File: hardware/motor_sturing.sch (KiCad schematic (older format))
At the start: 6 parts, among them U1 LTC2351-14, U22 LTC2351-14, U5 MAX6101

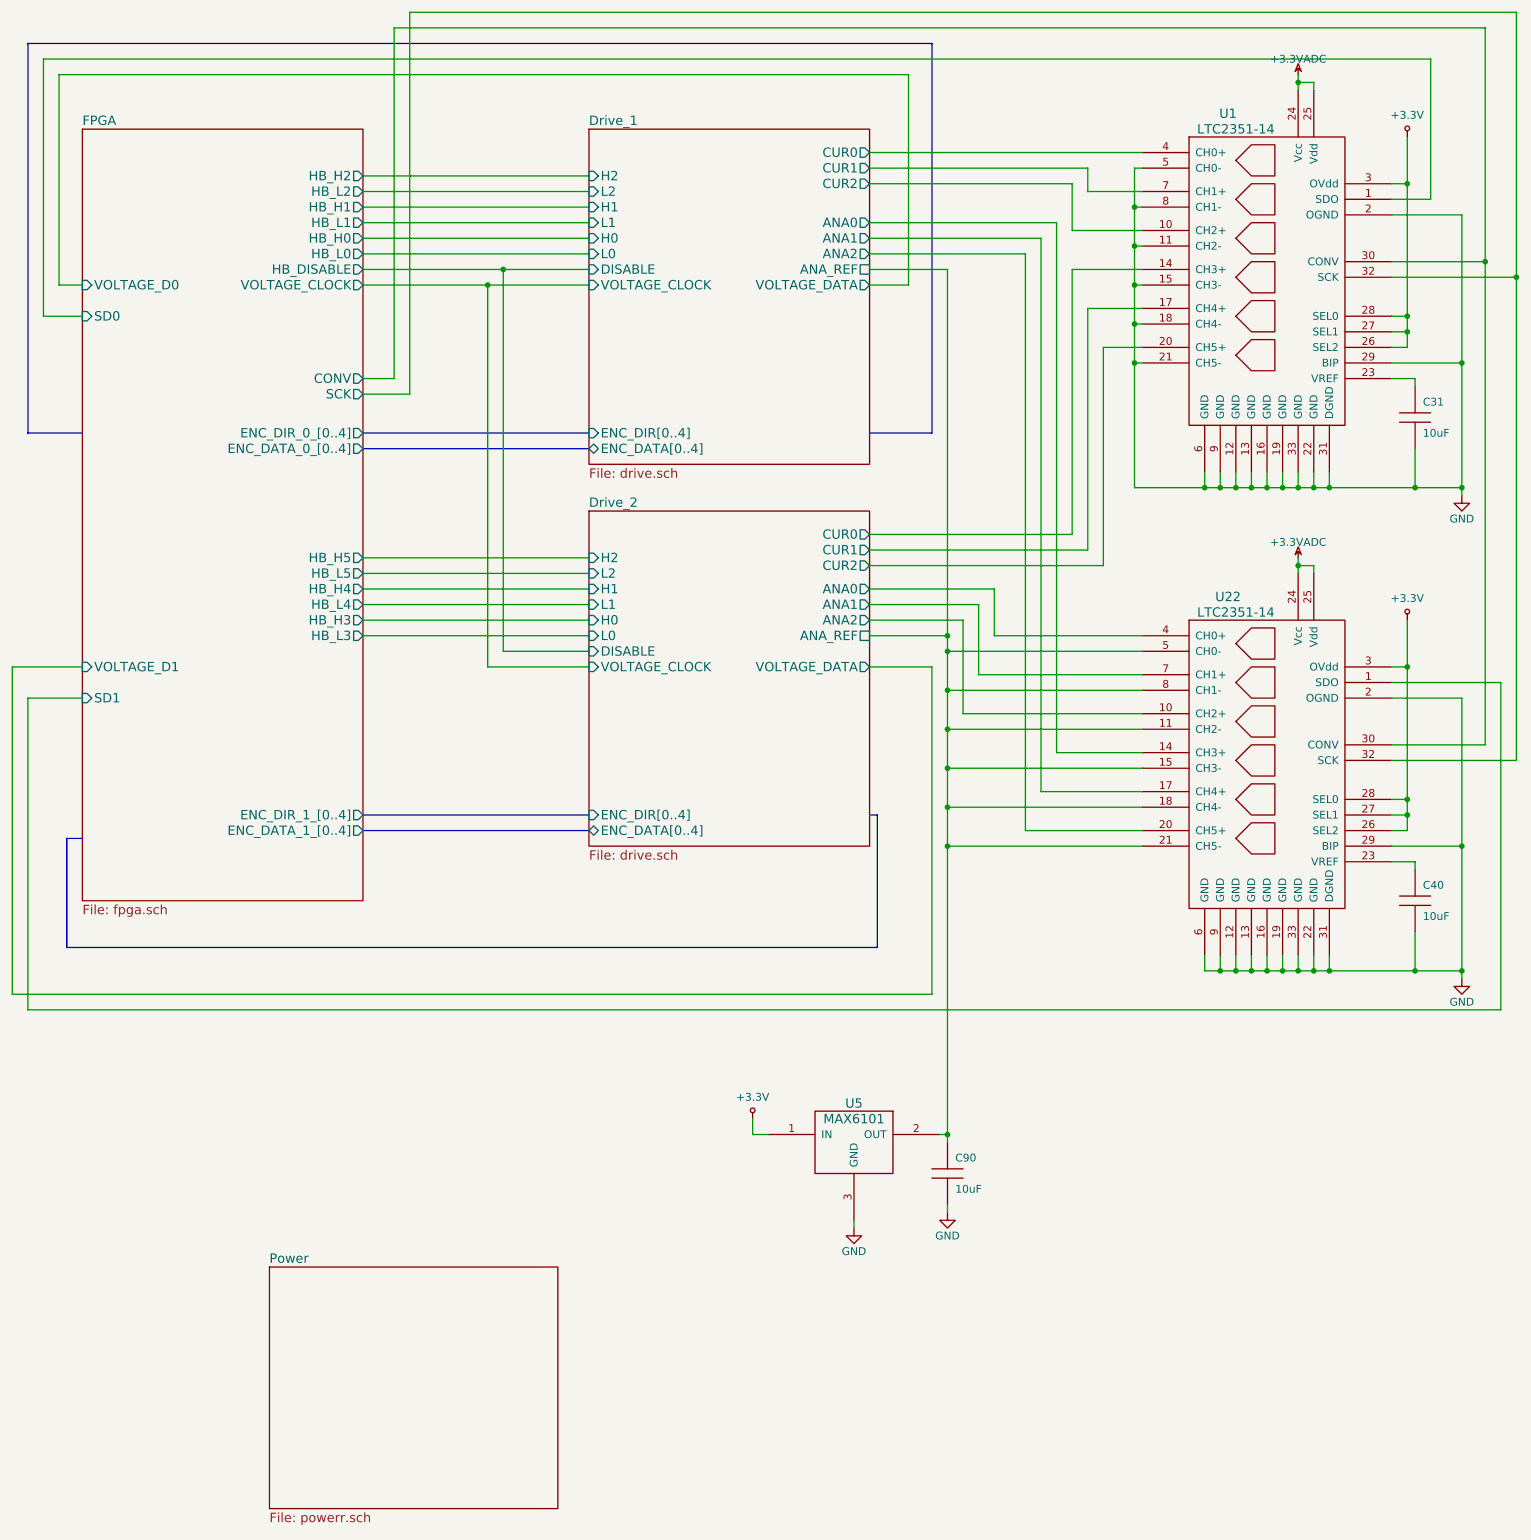
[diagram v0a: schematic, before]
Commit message: Backup, clearing bottom of power section.
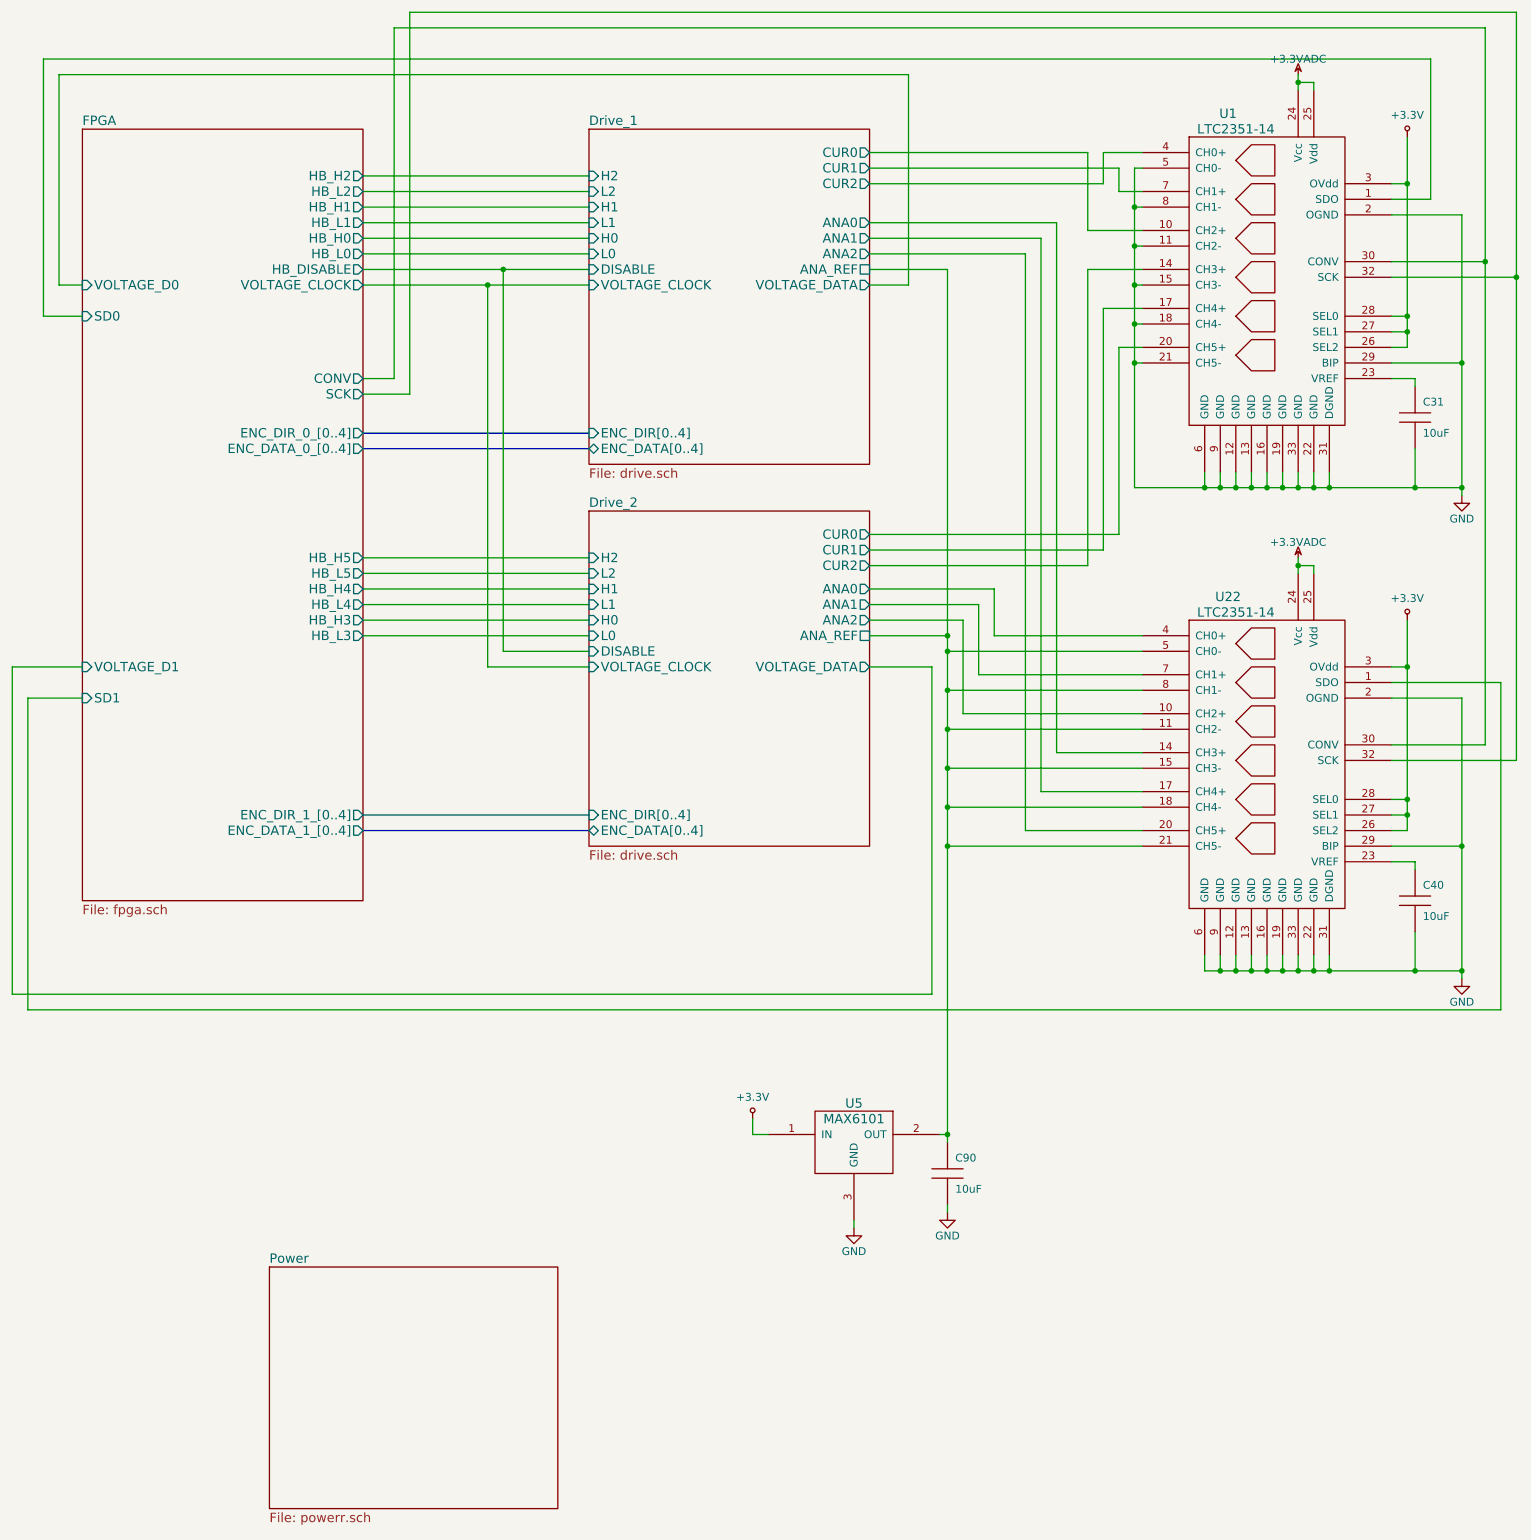
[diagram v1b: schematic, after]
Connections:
- net Drive_1/CUR0: now also U1.10 (CH2+); no longer U1.4 (CH0+)
- net Drive_1/CUR2: now also U1.4 (CH0+); no longer U1.10 (CH2+)
- net Drive_2/CUR0: now also U1.20 (CH5+); no longer U1.14 (CH3+)
- net Drive_2/CUR2: now also U1.14 (CH3+); no longer U1.20 (CH5+)
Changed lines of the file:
@@
 Wire Wire Line
 	4450 4700 5000 4700
-Wire Bus Line
-	6800 5750 6850 5750
-Wire Bus Line
-	6850 5750 6850 6600
-Wire Bus Line
-	6850 6600 1650 6600
-Wire Bus Line
-	1650 6600 1650 5900
-Wire Bus Line
-	1650 5900 1750 5900
 Wire Wire Line
 	1600 1000 1600 2350
@@
 Wire Wire Line
 	1500 2550 1750 2550
-Wire Bus Line
-	6800 3300 7200 3300
-Wire Bus Line
-	7200 3300 7200 800
-Wire Bus Line
-	7200 800  1400 800
-Wire Bus Line
-	1400 800  1400 3300
-Wire Bus Line
-	1400 3300 1750 3300
-Wire Wire Line
-	6800 1600 8200 1600
-Wire Wire Line
-	8200 1600 8200 1750
-Wire Wire Line
-	8200 1750 8550 1750
-Wire Wire Line
-	6800 1700 8100 1700
-Wire Wire Line
-	6800 3950 8100 3950
-Wire Wire Line
-	8100 3950 8100 2250
-Wire Wire Line
-	8100 2250 8550 2250
-Wire Wire Line
-	8100 1700 8100 2000
-Wire Wire Line
-	8100 2000 8550 2000
-Wire Wire Line
-	8550 2500 8200 2500
-Wire Wire Line
-	8200 2500 8200 4050
-Wire Wire Line
-	8200 4050 6800 4050
-Wire Wire Line
-	6800 4150 8300 4150
-Wire Wire Line
-	8300 4150 8300 2750
-Wire Wire Line
-	8300 2750 8550 2750
 Wire Wire Line
 	8550 1600 8500 1600
@@
 	8550 1850 8500 1850
 Connection ~ 8500 1850
-Wire Wire Line
-	8550 1500 6800 1500
-$Comp
-L +3.3VADC #PWR5
+$Comp
+L +3.3VADC #PWR198
 U 1 1 56D0AB8B
 P 9550 4100
-F 0 "#PWR5" H 9700 4050 50  0001 C CNN
+F 0 "#PWR198" H 9700 4050 50  0001 C CNN
 F 1 "+3.3VADC" H 9550 4200 50  0000 C CNN
 F 2 "" H 9550 4100 50  0000 C CNN
@@
 Connection ~ 9550 4150
 $Comp
-L +3.3V #PWR6
+L +3.3V #PWR199
 U 1 1 56D0BAED
 P 10250 1400
-F 0 "#PWR6" H 10250 1250 50  0001 C CNN
+F 0 "#PWR199" H 10250 1250 50  0001 C CNN
 F 1 "+3.3V" H 10250 1540 50  0000 C CNN
 F 2 "" H 10250 1400 50  0000 C CNN
@@
 	10250 1700 10150 1700
 $Comp
-L GND #PWR8
+L GND #PWR201
 U 1 1 56D0BF5F
 P 10600 3700
-F 0 "#PWR8" H 10600 3450 50  0001 C CNN
+F 0 "#PWR201" H 10600 3450 50  0001 C CNN
 F 1 "GND" H 10600 3550 50  0000 C CNN
 F 2 "" H 10600 3700 50  0000 C CNN
@@
 $EndComp
 $Comp
-L +3.3V #PWR7
+L +3.3V #PWR200
 U 1 1 56D10ACF
 P 10250 4500
-F 0 "#PWR7" H 10250 4350 50  0001 C CNN
+F 0 "#PWR200" H 10250 4350 50  0001 C CNN
 F 1 "+3.3V" H 10250 4640 50  0000 C CNN
 F 2 "" H 10250 4500 50  0000 C CNN
@@
 	10250 4800 10150 4800
 $Comp
-L GND #PWR9
+L GND #PWR202
 U 1 1 56D10AD7
 P 10600 6800
-F 0 "#PWR9" H 10600 6550 50  0001 C CNN
+F 0 "#PWR202" H 10600 6550 50  0001 C CNN
 F 1 "GND" H 10600 6650 50  0000 C CNN
 F 2 "" H 10600 6800 50  0000 C CNN
@@
 $EndComp
 $Comp
-L +3.3V #PWR1
+L +3.3V #PWR194
 U 1 1 56D1582B
 P 6050 7700
-F 0 "#PWR1" H 6050 7550 50  0001 C CNN
+F 0 "#PWR194" H 6050 7550 50  0001 C CNN
 F 1 "+3.3V" H 6050 7840 50  0000 C CNN
 F 2 "" H 6050 7700 50  0000 C CNN
@@
 	6050 7800 6150 7800
 $Comp
-L GND #PWR2
+L GND #PWR195
 U 1 1 56D15D96
 P 6700 8400
-F 0 "#PWR2" H 6700 8150 50  0001 C CNN
+F 0 "#PWR195" H 6700 8150 50  0001 C CNN
 F 1 "GND" H 6700 8250 50  0000 C CNN
 F 2 "" H 6700 8400 50  0000 C CNN
@@
 Connection ~ 10950 2300
 $Comp
-L +3.3VADC #PWR4
+L +3.3VADC #PWR197
 U 1 1 56D1B9BD
 P 9550 1000
-F 0 "#PWR4" H 9700 950 50  0001 C CNN
+F 0 "#PWR197" H 9700 950 50  0001 C CNN
 F 1 "+3.3VADC" H 9550 1100 50  0000 C CNN
 F 2 "" H 9550 1000 50  0000 C CNN
@@
 Connection ~ 7300 7800
 $Comp
-L GND #PWR3
+L GND #PWR196
 U 1 1 56D58C47
 P 7300 8300
-F 0 "#PWR3" H 7300 8050 50  0001 C CNN
+F 0 "#PWR196" H 7300 8050 50  0001 C CNN
 F 1 "GND" H 7300 8150 50  0000 C CNN
 F 2 "" H 7300 8300 50  0000 C CNN
@@
 Wire Wire Line
 	7300 8300 7300 8250
+Wire Wire Line
+	6800 1700 8300 1700
+Wire Wire Line
+	8300 1700 8300 1500
+Wire Wire Line
+	8300 1500 8550 1500
+Wire Wire Line
+	8550 1750 8400 1750
+Wire Wire Line
+	8400 1750 8400 1600
+Wire Wire Line
+	8400 1600 6800 1600
+Wire Wire Line
+	6800 1500 8200 1500
+Wire Wire Line
+	8200 1500 8200 2000
+Wire Wire Line
+	8200 2000 8550 2000
+Wire Wire Line
+	8550 2750 8400 2750
+Wire Wire Line
+	8400 2750 8400 3950
+Wire Wire Line
+	8400 3950 6800 3950
+Wire Wire Line
+	6800 4050 8300 4050
+Wire Wire Line
+	8300 4050 8300 2500
+Wire Wire Line
+	8300 2500 8550 2500
+Wire Wire Line
+	8550 2250 8200 2250
+Wire Wire Line
+	8200 2250 8200 4150
+Wire Wire Line
+	8200 4150 6800 4150
 $EndSCHEMATC

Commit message: Progress.
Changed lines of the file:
@@
 Connection ~ 8500 1850
 $Comp
-L +3.3VADC #PWR198
+L +3.3VADC #PWR218
 U 1 1 56D0AB8B
 P 9550 4100
-F 0 "#PWR198" H 9700 4050 50  0001 C CNN
+F 0 "#PWR218" H 9700 4050 50  0001 C CNN
 F 1 "+3.3VADC" H 9550 4200 50  0000 C CNN
 F 2 "" H 9550 4100 50  0000 C CNN
@@
 	9650 4150 9650 4200
 Connection ~ 9550 4150
-$Comp
-L +3.3V #PWR199
-U 1 1 56D0BAED
-P 10250 1400
-F 0 "#PWR199" H 10250 1250 50  0001 C CNN
-F 1 "+3.3V" H 10250 1540 50  0000 C CNN
-F 2 "" H 10250 1400 50  0000 C CNN
-F 3 "" H 10250 1400 50  0000 C CNN
-	1    10250 1400
-	1    0    0    -1
-$EndComp
 Wire Wire Line
 	10250 1400 10250 2750
@@
 	10250 1700 10150 1700
 $Comp
-L GND #PWR201
+L GND #PWR221
 U 1 1 56D0BF5F
 P 10600 3700
-F 0 "#PWR201" H 10600 3450 50  0001 C CNN
+F 0 "#PWR221" H 10600 3450 50  0001 C CNN
 F 1 "GND" H 10600 3550 50  0000 C CNN
 F 2 "" H 10600 3700 50  0000 C CNN
@@
 	1    0    0    -1
 $EndComp
-$Comp
-L +3.3V #PWR200
-U 1 1 56D10ACF
-P 10250 4500
-F 0 "#PWR200" H 10250 4350 50  0001 C CNN
-F 1 "+3.3V" H 10250 4640 50  0000 C CNN
-F 2 "" H 10250 4500 50  0000 C CNN
-F 3 "" H 10250 4500 50  0000 C CNN
-	1    10250 4500
-	1    0    0    -1
-$EndComp
 Wire Wire Line
 	10250 4500 10250 5850
@@
 	10250 4800 10150 4800
 $Comp
-L GND #PWR202
+L GND #PWR222
 U 1 1 56D10AD7
 P 10600 6800
-F 0 "#PWR202" H 10600 6550 50  0001 C CNN
+F 0 "#PWR222" H 10600 6550 50  0001 C CNN
 F 1 "GND" H 10600 6650 50  0000 C CNN
 F 2 "" H 10600 6800 50  0000 C CNN
@@
 	1    0    0    -1
 $EndComp
-$Comp
-L +3.3V #PWR194
-U 1 1 56D1582B
-P 6050 7700
-F 0 "#PWR194" H 6050 7550 50  0001 C CNN
-F 1 "+3.3V" H 6050 7840 50  0000 C CNN
-F 2 "" H 6050 7700 50  0000 C CNN
-F 3 "" H 6050 7700 50  0000 C CNN
-	1    6050 7700
-	1    0    0    -1
-$EndComp
 Wire Wire Line
 	6050 7700 6050 7800
@@
 	6050 7800 6150 7800
 $Comp
-L GND #PWR195
+L GND #PWR215
 U 1 1 56D15D96
 P 6700 8400
-F 0 "#PWR195" H 6700 8150 50  0001 C CNN
+F 0 "#PWR215" H 6700 8150 50  0001 C CNN
 F 1 "GND" H 6700 8250 50  0000 C CNN
 F 2 "" H 6700 8400 50  0000 C CNN
@@
 Connection ~ 10950 2300
 $Comp
-L +3.3VADC #PWR197
+L +3.3VADC #PWR217
 U 1 1 56D1B9BD
 P 9550 1000
-F 0 "#PWR197" H 9700 950 50  0001 C CNN
+F 0 "#PWR217" H 9700 950 50  0001 C CNN
 F 1 "+3.3VADC" H 9550 1100 50  0000 C CNN
 F 2 "" H 9550 1000 50  0000 C CNN
@@
 Connection ~ 7300 7800
 $Comp
-L GND #PWR196
+L GND #PWR216
 U 1 1 56D58C47
 P 7300 8300
-F 0 "#PWR196" H 7300 8050 50  0001 C CNN
+F 0 "#PWR216" H 7300 8050 50  0001 C CNN
 F 1 "GND" H 7300 8150 50  0000 C CNN
 F 2 "" H 7300 8300 50  0000 C CNN
@@
 Wire Wire Line
 	8200 4150 6800 4150
+$Comp
+L +3.3V #PWR214
+U 1 1 56DB5355
+P 6050 7700
+F 0 "#PWR214" H 6100 7730 20  0001 C CNN
+F 1 "+3.3V" H 6050 7790 30  0000 C CNN
+F 2 "" H 6050 7700 60  0000 C CNN
+F 3 "" H 6050 7700 60  0000 C CNN
+	1    6050 7700
+	1    0    0    -1
+$EndComp
+$Comp
+L +3.3V #PWR219
+U 1 1 56DBFBBB
+P 10250 1400
+F 0 "#PWR219" H 10300 1430 20  0001 C CNN
+F 1 "+3.3V" H 10250 1490 30  0000 C CNN
+F 2 "" H 10250 1400 60  0000 C CNN
+F 3 "" H 10250 1400 60  0000 C CNN
+	1    10250 1400
+	1    0    0    -1
+$EndComp
+$Comp
+L +3.3V #PWR220
+U 1 1 56DC019F
+P 10250 4500
+F 0 "#PWR220" H 10300 4530 20  0001 C CNN
+F 1 "+3.3V" H 10250 4590 30  0000 C CNN
+F 2 "" H 10250 4500 60  0000 C CNN
+F 3 "" H 10250 4500 60  0000 C CNN
+	1    10250 4500
+	1    0    0    -1
+$EndComp
 $EndSCHEMATC

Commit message: Backup
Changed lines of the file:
@@
 F19 "SD0" I L 1750 2550 60
 F20 "SD1" I L 1750 5000 60
-F21 "HB_DISABLE" O R 3550 2250 60
-F22 "ENC_DATA_0_[0..4]" O R 3550 3400 60
-F23 "ENC_DIR_0_[0..4]" O R 3550 3300 60
-F24 "ENC_DATA_1_[0..4]" O R 3550 5850 60
-F25 "ENC_DIR_1_[0..4]" O R 3550 5750 60
+F21 "ENC_DATA_0_[0..4]" O R 3550 3400 60
+F22 "ENC_DIR_0_[0..4]" O R 3550 3300 60
+F23 "ENC_DATA_1_[0..4]" O R 3550 5850 60
+F24 "ENC_DIR_1_[0..4]" O R 3550 5750 60
 $EndSheet
 $Sheet
@@
 F8 "VOLTAGE_CLOCK" I L 5000 2350 60
 F9 "VOLTAGE_DATA" O R 6800 2350 60
-F10 "DISABLE" I L 5000 2250 60
-F11 "CUR0" O R 6800 1500 60
-F12 "CUR1" O R 6800 1600 60
-F13 "CUR2" O R 6800 1700 60
-F14 "ANA0" O R 6800 1950 60
-F15 "ANA1" O R 6800 2050 60
-F16 "ANA2" O R 6800 2150 60
-F17 "ANA_REF" U R 6800 2250 60
-F18 "ENC_DIR[0..4]" I L 5000 3300 60
-F19 "ENC_DATA[0..4]" B L 5000 3400 60
+F10 "CUR0" O R 6800 1500 60
+F11 "CUR1" O R 6800 1600 60
+F12 "CUR2" O R 6800 1700 60
+F13 "ANA0" O R 6800 1950 60
+F14 "ANA1" O R 6800 2050 60
+F15 "ANA2" O R 6800 2150 60
+F16 "ANA_REF" U R 6800 2250 60
+F17 "ENC_DIR[0..4]" I L 5000 3300 60
+F18 "ENC_DATA[0..4]" B L 5000 3400 60
 $EndSheet
 $Sheet
@@
 F8 "VOLTAGE_CLOCK" I L 5000 4800 60
 F9 "VOLTAGE_DATA" O R 6800 4800 60
-F10 "DISABLE" I L 5000 4700 60
-F11 "CUR0" O R 6800 3950 60
-F12 "CUR1" O R 6800 4050 60
-F13 "CUR2" O R 6800 4150 60
-F14 "ANA0" O R 6800 4300 60
-F15 "ANA1" O R 6800 4400 60
-F16 "ANA2" O R 6800 4500 60
-F17 "ANA_REF" U R 6800 4600 60
-F18 "ENC_DIR[0..4]" I L 5000 5750 60
-F19 "ENC_DATA[0..4]" B L 5000 5850 60
+F10 "CUR0" O R 6800 3950 60
+F11 "CUR1" O R 6800 4050 60
+F12 "CUR2" O R 6800 4150 60
+F13 "ANA0" O R 6800 4300 60
+F14 "ANA1" O R 6800 4400 60
+F15 "ANA2" O R 6800 4500 60
+F16 "ANA_REF" U R 6800 4600 60
+F17 "ENC_DIR[0..4]" I L 5000 5750 60
+F18 "ENC_DATA[0..4]" B L 5000 5850 60
 $EndSheet
 $Comp
@@
 	5000 5850 3550 5850
 Wire Wire Line
-	4450 4700 4450 2250
-Wire Wire Line
-	3550 2250 5000 2250
-Connection ~ 4450 2250
-Wire Wire Line
-	4450 4700 5000 4700
-Wire Wire Line
 	1600 1000 1600 2350
 Wire Wire Line
@@
 Connection ~ 8500 1850
 $Comp
-L +3.3VADC #PWR218
+L +3.3VADC #PWR5
 U 1 1 56D0AB8B
 P 9550 4100
-F 0 "#PWR218" H 9700 4050 50  0001 C CNN
+F 0 "#PWR5" H 9700 4050 50  0001 C CNN
 F 1 "+3.3VADC" H 9550 4200 50  0000 C CNN
 F 2 "" H 9550 4100 50  0000 C CNN
@@
 	10250 1700 10150 1700
 $Comp
-L GND #PWR221
+L GND #PWR8
 U 1 1 56D0BF5F
 P 10600 3700
-F 0 "#PWR221" H 10600 3450 50  0001 C CNN
+F 0 "#PWR8" H 10600 3450 50  0001 C CNN
 F 1 "GND" H 10600 3550 50  0000 C CNN
 F 2 "" H 10600 3700 50  0000 C CNN
@@
 	10250 4800 10150 4800
 $Comp
-L GND #PWR222
+L GND #PWR9
 U 1 1 56D10AD7
 P 10600 6800
-F 0 "#PWR222" H 10600 6550 50  0001 C CNN
+F 0 "#PWR9" H 10600 6550 50  0001 C CNN
 F 1 "GND" H 10600 6650 50  0000 C CNN
 F 2 "" H 10600 6800 50  0000 C CNN
@@
 	6050 7800 6150 7800
 $Comp
-L GND #PWR215
+L GND #PWR2
 U 1 1 56D15D96
 P 6700 8400
-F 0 "#PWR215" H 6700 8150 50  0001 C CNN
+F 0 "#PWR2" H 6700 8150 50  0001 C CNN
 F 1 "GND" H 6700 8250 50  0000 C CNN
 F 2 "" H 6700 8400 50  0000 C CNN
@@
 Connection ~ 10950 2300
 $Comp
-L +3.3VADC #PWR217
+L +3.3VADC #PWR4
 U 1 1 56D1B9BD
 P 9550 1000
-F 0 "#PWR217" H 9700 950 50  0001 C CNN
+F 0 "#PWR4" H 9700 950 50  0001 C CNN
 F 1 "+3.3VADC" H 9550 1100 50  0000 C CNN
 F 2 "" H 9550 1000 50  0000 C CNN
@@
 Connection ~ 7300 7800
 $Comp
-L GND #PWR216
+L GND #PWR3
 U 1 1 56D58C47
 P 7300 8300
-F 0 "#PWR216" H 7300 8050 50  0001 C CNN
+F 0 "#PWR3" H 7300 8050 50  0001 C CNN
 F 1 "GND" H 7300 8150 50  0000 C CNN
 F 2 "" H 7300 8300 50  0000 C CNN
@@
 	8200 4150 6800 4150
 $Comp
-L +3.3V #PWR214
+L +3.3V #PWR1
 U 1 1 56DB5355
 P 6050 7700
-F 0 "#PWR214" H 6100 7730 20  0001 C CNN
+F 0 "#PWR1" H 6100 7730 20  0001 C CNN
 F 1 "+3.3V" H 6050 7790 30  0000 C CNN
 F 2 "" H 6050 7700 60  0000 C CNN
@@
 $EndComp
 $Comp
-L +3.3V #PWR219
+L +3.3V #PWR6
 U 1 1 56DBFBBB
 P 10250 1400
-F 0 "#PWR219" H 10300 1430 20  0001 C CNN
+F 0 "#PWR6" H 10300 1430 20  0001 C CNN
 F 1 "+3.3V" H 10250 1490 30  0000 C CNN
 F 2 "" H 10250 1400 60  0000 C CNN
@@
 $EndComp
 $Comp
-L +3.3V #PWR220
+L +3.3V #PWR7
 U 1 1 56DC019F
 P 10250 4500
-F 0 "#PWR220" H 10300 4530 20  0001 C CNN
+F 0 "#PWR7" H 10300 4530 20  0001 C CNN
 F 1 "+3.3V" H 10250 4590 30  0000 C CNN
 F 2 "" H 10250 4500 60  0000 C CNN
